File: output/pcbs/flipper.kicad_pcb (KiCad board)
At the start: 2 copper layers, 149.6 x 110.4 mm, 60 parts

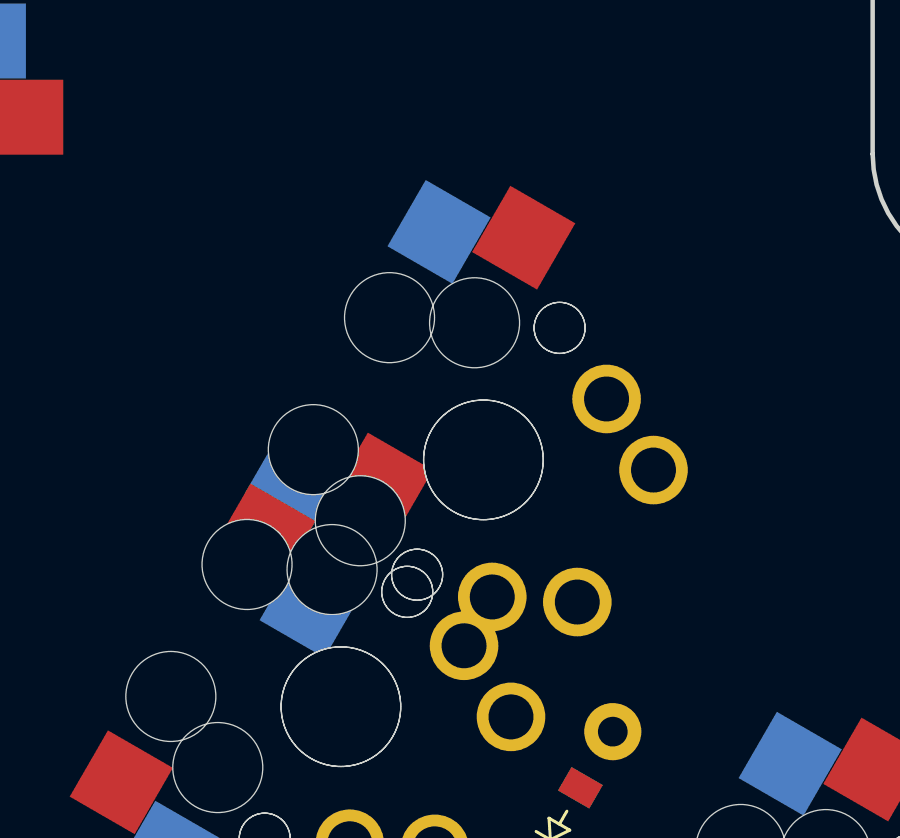
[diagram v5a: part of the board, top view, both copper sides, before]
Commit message: remove optional
remove optional key due to insufficient size
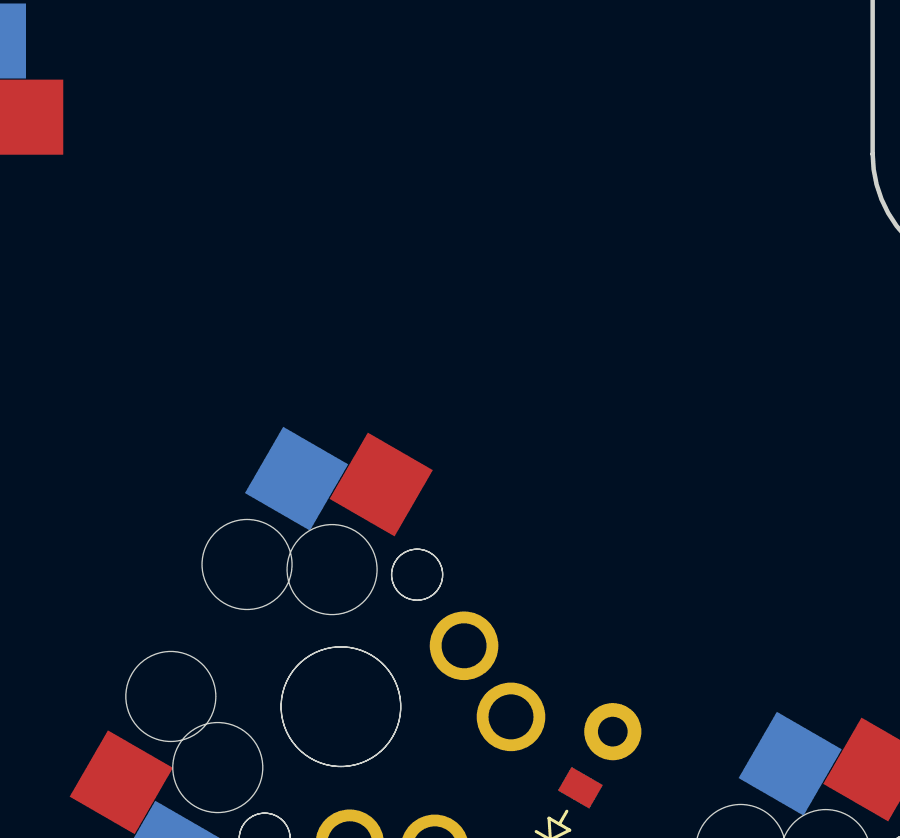
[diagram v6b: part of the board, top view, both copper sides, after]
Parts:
- removed S37, S38: , MX
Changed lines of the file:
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@@
         (pad 2 thru_hole circle (at 3.81 0 60) (size 1.905 1.905) (drill 0.9906) (layers *.Cu *.Mask) (net 23 "reach_cluster"))
     )
-      (module MX (layer F.Cu)
-      (at 208.2029287 84.8910233 240)
-      (fp_text reference "S37" (at 0 0) (layer F.SilkS) hide (effects (font (size 1.27 1.27) (thickness 0.15))))
-      (fp_text value "" (at 0 0) (layer F.SilkS) hide (effects (font (size 1.27 1.27) (thickness 0.15))))
-      (fp_line (start -7 -6) (end -7 -7) (layer Dwgs.User) (width 0.15))
-      (fp_line (start -7 7) (end -6 7) (layer Dwgs.User) (width 0.15))
-      (fp_line (start -6 -7) (end -7 -7) (layer Dwgs.User) (width 0.15))
-      (fp_line (start -7 7) (end -7 6) (layer Dwgs.User) (width 0.15))
-      (fp_line (start 7 6) (end 7 7) (layer Dwgs.User) (width 0.15))
-      (fp_line (start 7 -7) (end 6 -7) (layer Dwgs.User) (width 0.15))
-      (fp_line (start 6 7) (end 7 7) (layer Dwgs.User) (width 0.15))
-      (fp_line (start 7 -7) (end 7 -6) (layer Dwgs.User) (width 0.15))
-      (pad "" np_thru_hole circle (at 0 0) (size 3.9878 3.9878) (drill 3.9878) (layers *.Cu *.Mask))
-      (pad "" np_thru_hole circle (at 5.08 0) (size 1.7018 1.7018) (drill 1.7018) (layers *.Cu *.Mask))
-      (pad "" np_thru_hole circle (at -5.08 0) (size 1.7018 1.7018) (drill 1.7018) (layers *.Cu *.Mask))
-      (fp_line (start -9.5 -9.5) (end 9.5 -9.5) (layer Dwgs.User) (width 0.15))
-      (fp_line (start 9.5 -9.5) (end 9.5 9.5) (layer Dwgs.User) (width 0.15))
-      (fp_line (start 9.5 9.5) (end -9.5 9.5) (layer Dwgs.User) (width 0.15))
-      (fp_line (start -9.5 9.5) (end -9.5 -9.5) (layer Dwgs.User) (width 0.15))
-            (pad 1 thru_hole circle (at 2.54 -5.08) (size 2.286 2.286) (drill 1.4986) (layers *.Cu *.Mask) (net 13 "P18"))
-            (pad 2 thru_hole circle (at -3.81 -2.54) (size 2.286 2.286) (drill 1.4986) (layers *.Cu *.Mask) (net 22 "middle_cluster"))
-            (pad 1 thru_hole circle (at -2.54 -5.08) (size 2.286 2.286) (drill 1.4986) (layers *.Cu *.Mask) (net 13 "P18"))
-            (pad 2 thru_hole circle (at 3.81 -2.54) (size 2.286 2.286) (drill 1.4986) (layers *.Cu *.Mask) (net 22 "middle_cluster"))
-          )
-      (module MX (layer F.Cu)
-      (at 208.2029287 84.8910233 60)
-      (fp_text reference "S38" (at 0 0) (layer F.SilkS) hide (effects (font (size 1.27 1.27) (thickness 0.15))))
-      (fp_text value "" (at 0 0) (layer F.SilkS) hide (effects (font (size 1.27 1.27) (thickness 0.15))))
-      (fp_line (start -7 -6) (end -7 -7) (layer Dwgs.User) (width 0.15))
-      (fp_line (start -7 7) (end -6 7) (layer Dwgs.User) (width 0.15))
-      (fp_line (start -6 -7) (end -7 -7) (layer Dwgs.User) (width 0.15))
-      (fp_line (start -7 7) (end -7 6) (layer Dwgs.User) (width 0.15))
-      (fp_line (start 7 6) (end 7 7) (layer Dwgs.User) (width 0.15))
-      (fp_line (start 7 -7) (end 6 -7) (layer Dwgs.User) (width 0.15))
-      (fp_line (start 6 7) (end 7 7) (layer Dwgs.User) (width 0.15))
-      (fp_line (start 7 -7) (end 7 -6) (layer Dwgs.User) (width 0.15))
-      (pad "" np_thru_hole circle (at 0 0) (size 3.9878 3.9878) (drill 3.9878) (layers *.Cu *.Mask))
-      (pad "" np_thru_hole circle (at 5.08 0) (size 1.7018 1.7018) (drill 1.7018) (layers *.Cu *.Mask))
-      (pad "" np_thru_hole circle (at -5.08 0) (size 1.7018 1.7018) (drill 1.7018) (layers *.Cu *.Mask))
-      (fp_line (start -9.5 -9.5) (end 9.5 -9.5) (layer Dwgs.User) (width 0.15))
-      (fp_line (start 9.5 -9.5) (end 9.5 9.5) (layer Dwgs.User) (width 0.15))
-      (fp_line (start 9.5 9.5) (end -9.5 9.5) (layer Dwgs.User) (width 0.15))
-      (fp_line (start -9.5 9.5) (end -9.5 -9.5) (layer Dwgs.User) (width 0.15))
-        (pad "" np_thru_hole circle (at 2.54 -5.08) (size 3 3) (drill 3) (layers *.Cu *.Mask))
-        (pad "" np_thru_hole circle (at -3.81 -2.54) (size 3 3) (drill 3) (layers *.Cu *.Mask))
-        (pad 1 smd rect (at -7.085 -2.54 60) (size 2.55 2.5) (layers B.Cu B.Paste B.Mask) (net 13 "P18"))
-        (pad 2 smd rect (at 5.842 -5.08 60) (size 2.55 2.5) (layers B.Cu B.Paste B.Mask) (net 22 "middle_cluster"))
-        (pad "" np_thru_hole circle (at -2.54 -5.08) (size 3 3) (drill 3) (layers *.Cu *.Mask))
-        (pad "" np_thru_hole circle (at 3.81 -2.54) (size 3 3) (drill 3) (layers *.Cu *.Mask))
-        (pad 1 smd rect (at 7.085 -2.54 60) (size 2.55 2.5) (layers F.Cu F.Paste F.Mask) (net 13 "P18"))
-        (pad 2 smd rect (at -5.842 -5.08 60) (size 2.55 2.5) (layers F.Cu F.Paste F.Mask) (net 22 "middle_cluster"))
-        )
   (footprint "ceoloide:mcu_nice_nano"
     (layer "F.Cu")

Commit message: working with custom reversible pimoroni
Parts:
- added ?: , pimoroni_trackball, F.Cu at (152.6, 78.9)
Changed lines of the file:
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@@
 (net 69 "JST1_1")
 (net 70 "JST1_2")
+(net 71 "INT")
   (net_class Default "This is the default net class."
     (clearance 0.2)
@@
 (add_net "JST1_1")
 (add_net "JST1_2")
+(add_net "INT")
   )
       (module MX (layer F.Cu)
@@
     (pad "1" thru_hole circle (at 3.25 0 90) (size 2 2) (drill 1.3) (layers "*.Cu" "*.Mask") (net 30 "RST"))
   )
+      (module pimoroni_trackball (layer F.Cu)
+      (at 152.5874943 78.8582761 -90)
+        (descr "Pimoroni I2C trackball breakout")
+        (tags "Through hole pin header THT 1x05 2.54mm single row")
+        (fp_line (start -1.8 -1.8) (end -1.8 11.95) (layer F.CrtYd) (width 0.05))
+        (fp_line (start -1.8 11.95) (end 1.8 11.95) (layer F.CrtYd) (width 0.05))
+        (fp_line (start 1.8 11.95) (end 1.8 -1.8) (layer F.CrtYd) (width 0.05))
+        (fp_line (start 1.8 -1.8) (end -1.8 -1.8) (layer F.CrtYd) (width 0.05))
+        (fp_line (start -1.5 -2.6) (end -1.5 12.5) (layer F.SilkS) (width 0.12))
+        (fp_line (start -1.5 12.5) (end 4.5 12.5) (layer F.SilkS) (width 0.12))
+        (fp_line (start 4.5 12.5) (end 4.5 17.5) (layer F.SilkS) (width 0.12))
+        (fp_line (start 4.5 17.5) (end 20.5 17.5) (layer F.SilkS) (width 0.12))
+        (fp_line (start -1.5 -2.6) (end 4.5 -2.6) (layer F.SilkS) (width 0.12))
+        (fp_line (start 4.5 -7.6) (end 20.5 -7.6) (layer F.SilkS) (width 0.12))
+        (fp_line (start 4.5 -2.6) (end 4.5 -7.6) (layer F.SilkS) (width 0.12))
+        (fp_line (start 20.5 17.5) (end 20.5 -7.6) (layer F.SilkS) (width 0.12))
+        (fp_line (start -1.8 -1.8) (end -1.8 11.95) (layer B.CrtYd) (width 0.05))
+        (fp_line (start -1.8 11.95) (end 1.8 11.95) (layer B.CrtYd) (width 0.05))
+        (fp_line (start 1.8 11.95) (end 1.8 -1.8) (layer B.CrtYd) (width 0.05))
+        (fp_line (start 1.8 -1.8) (end -1.8 -1.8) (layer B.CrtYd) (width 0.05))
+        (fp_line (start -1.5 -2.6) (end -1.5 12.5) (layer B.SilkS) (width 0.12))
+        (fp_line (start -1.5 12.5) (end 4.5 12.5) (layer B.SilkS) (width 0.12))
+        (fp_line (start 4.5 12.5) (end 4.5 17.5) (layer B.SilkS) (width 0.12))
+        (fp_line (start 4.5 17.5) (end 20.5 17.5) (layer B.SilkS) (width 0.12))
+        (fp_line (start -1.5 -2.6) (end 4.5 -2.6) (layer B.SilkS) (width 0.12))
+        (fp_line (start 4.5 -7.6) (end 20.5 -7.6) (layer B.SilkS) (width 0.12))
+        (fp_line (start 4.5 -2.6) (end 4.5 -7.6) (layer B.SilkS) (width 0.12))
+        (fp_line (start 20.5 17.5) (end 20.5 -7.6) (layer B.SilkS) (width 0.12))
+        (pad 1 np_thru_hole circle (at 7.05 14.7) (size 2.5 2.5) (drill 2.5) (layers *.Cu *.Mask))
+        (pad 2 np_thru_hole circle (at 17.95 14.7) (size 2.5 2.5) (drill 2.5) (layers *.Cu *.Mask))
+        (pad 3 np_thru_hole circle (at 17.95 -4.9) (size 2.5 2.5) (drill 2.5) (layers *.Cu *.Mask))
+        (pad 4 np_thru_hole circle (at 7.05 -4.9) (size 2.5 2.5) (drill 2.5) (layers *.Cu *.Mask))
+        (pad 1 thru_hole oval (at 0 0 0) (size 1.7 1.7) (drill 1) (layers *.Cu *.Mask) (net 31 "VCC"))
+        (pad 2 thru_hole oval (at 0 2.54) (size 1.7 1.7) (drill 1) (layers *.Cu *.Mask) (net 34 "P2"))
+        (pad 3 thru_hole oval (at 0 5.08) (size 1.7 1.7) (drill 1) (layers *.Cu *.Mask) (net 35 "P3"))
+        (pad 4 thru_hole oval (at 0 7.62) (size 1.7 1.7) (drill 1) (layers *.Cu *.Mask) (net 71 "INT"))
+        (pad 5 thru_hole oval (at 0 10.16) (size 1.7 1.7) (drill 1) (layers *.Cu *.Mask) (net 29 "GND"))
+        (fp_text user VCC (at 3 0 -90 ) (layer F.SilkS) (effects (font (size 0.8 0.8) (thickness 0.15))))
+        (fp_text user SDA (at 3 2.54 -90 ) (layer F.SilkS) (effects (font (size 0.8 0.8) (thickness 0.15))))
+        (fp_text user SCL (at 3 5.08 -90 ) (layer F.SilkS) (effects (font (size 0.8 0.8) (thickness 0.15))))
+        (fp_text user INT (at 3 7.62 -90 ) (layer F.SilkS) (effects (font (size 0.8 0.8) (thickness 0.15))))
+        (fp_text user GND (at 3 10.16 -90 ) (layer F.SilkS) (effects (font (size 0.8 0.8) (thickness 0.15))))
+        (fp_text user GND (at 3 0 -90 ) (layer B.SilkS) (effects (font (size 0.8 0.8) (thickness 0.15))(justify mirror)))
+        (fp_text user INT (at 3 2.54 -90 ) (layer B.SilkS) (effects (font (size 0.8 0.8) (thickness 0.15))(justify mirror)))
+        (fp_text user SCL (at 3 5.08 -90 ) (layer B.SilkS) (effects (font (size 0.8 0.8) (thickness 0.15))(justify mirror)))
+        (fp_text user SDA (at 3 7.62 -90 ) (layer B.SilkS) (effects (font (size 0.8 0.8) (thickness 0.15))(justify mirror)))
+        (fp_text user VCC (at 3 10.16 -90 ) (layer B.SilkS) (effects (font (size 0.8 0.8) (thickness 0.15))(justify mirror)))
+        (pad "21" smd custom (at 5 0 -180) (size 0.1 0.1) (layers "F.Cu" "F.Mask" "F.Paste")
+            (clearance 0.1) (zone_connect 0)
+            (options (clearance outline) (anchor rect))
+            (primitives
+                (gr_poly
+                    (pts
+                        (xy 0.6 0.4)
+                        (xy -0.6 0.4)
+                        (xy -0.6 0.2)
+                        (xy 0 -0.4)
+                        (xy 0.6 0.2)
+                    )
+                    (width 0)
+                    (fill yes)
+                )
+            )
+            (net 31 "VCC")
+        )
+        (pad "31" smd custom (at 5 0 -180) (size 0.1 0.1) (layers "B.Cu" "B.Mask" "B.Paste")
+            (clearance 0.1) (zone_connect 0)
+            (options (clearance outline) (anchor rect))
+            (primitives
+                (gr_poly
+                    (pts
+                        (xy 0.6 0.4)
+                        (xy -0.6 0.4)
+                        (xy -0.6 0.2)
+                        (xy 0 -0.4)
+                        (xy 0.6 0.2)
+                    )
+                    (width 0)
+                    (fill yes)
+                )
+            )
+            (net 29 "GND")
+        )
+        (pad "1" smd custom (at 6 0 -180) (size 1.2 0.5) (layers "F.Cu" "F.Mask" "F.Paste") (net 31 "VCC")
+            (clearance 0.1) (zone_connect 0)
+            (options (clearance outline) (anchor rect))
+            (primitives
+                (gr_poly
+                    (pts
+                        (xy 0.6 0)
+                        (xy -0.6 0)
+                        (xy -0.6 1)
+                        (xy 0 0.4)
+                        (xy 0.6 1)
+                    )
+                    (width 0)
+                    (fill yes)
+                )
+            )
+        )
+        (pad "1" smd custom (at 6 0 -180) (size 1.2 0.5) (layers "B.Cu" "B.Mask" "B.Paste") (net 29 "GND")
+            (clearance 0.1) (zone_connect 0)
+            (options (clearance outline) (anchor rect))
+            (primitives
+                (gr_poly
+                    (pts
+                        (xy 0.6 0)
+                        (xy -0.6 0)
+                        (xy -0.6 1)
+                        (xy 0 0.4)
+                        (xy 0.6 1)
+                    )
+                    (width 0)
+                    (fill yes)
+                )
+            )
+        )
+      )
   (gr_line (start 101.4026967 97.6197628) (end 119.7648005 95.36518) (angle 90) (layer Eco1.User) (width 0.15))
 (gr_line (start 119.7648005 95.36518) (end 117.5102177 77.0030762) (angle 90) (layer Eco1.User) (width 0.15))
